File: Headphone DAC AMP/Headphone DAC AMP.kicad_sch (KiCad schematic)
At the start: 0 parts

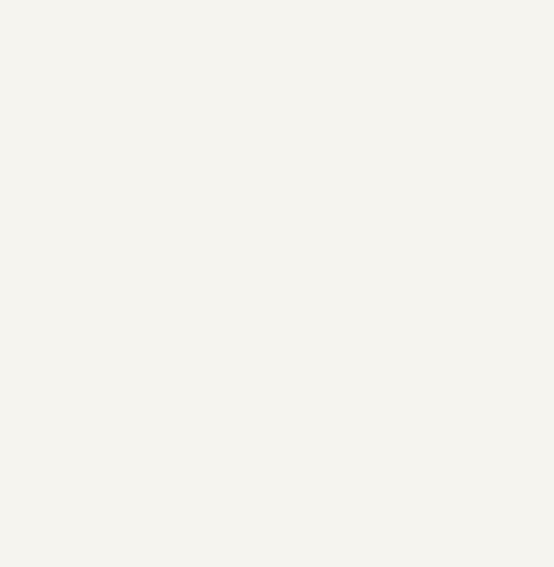
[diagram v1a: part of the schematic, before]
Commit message: Added crystals
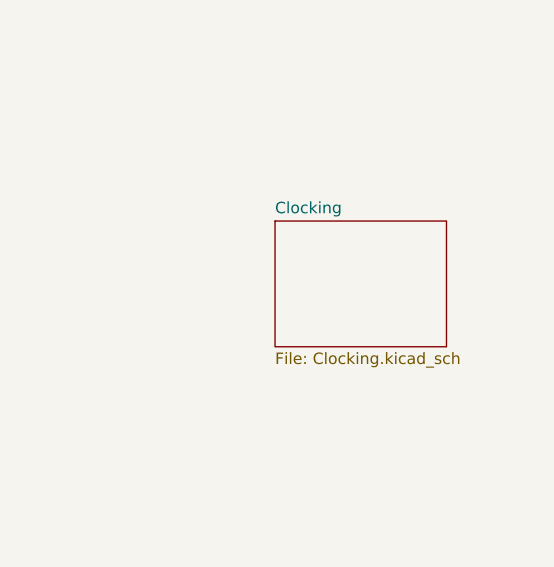
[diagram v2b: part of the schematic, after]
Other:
- added sheet Clocking (Clocking.kicad_sch)
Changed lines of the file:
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@@
+		)
+	)
+	(sheet
+		(at 203.2 72.39)
+		(size 19.05 13.97)
+		(exclude_from_sim no)
+		(in_bom yes)
+		(on_board yes)
+		(dnp no)
+		(fields_autoplaced yes)
+		(stroke
+			(width 0.1524)
+			(type solid)
+		)
+		(fill
+			(color 0 0 0 0.0000)
+		)
+		(property "Sheetname" "Clocking"
+			(at 203.2 71.6784 0)
+			(effects
+				(font
+					(size 1.27 1.27)
+				)
+				(justify left bottom)
+			)
+		)
+		(property "Sheetfile" "Clocking.kicad_sch"
+			(at 203.2 86.9446 0)
+			(effects
+				(font
+					(size 1.27 1.27)
+				)
+				(justify left top)
+			)
+		)
+		(instances
+			(project "Headphone DAC AMP"
+				(path "/d034eddd-efbc-47be-a25c-37cbfbab4cd8"
+					(page "7")
+				)
+			)
 		)
 	)

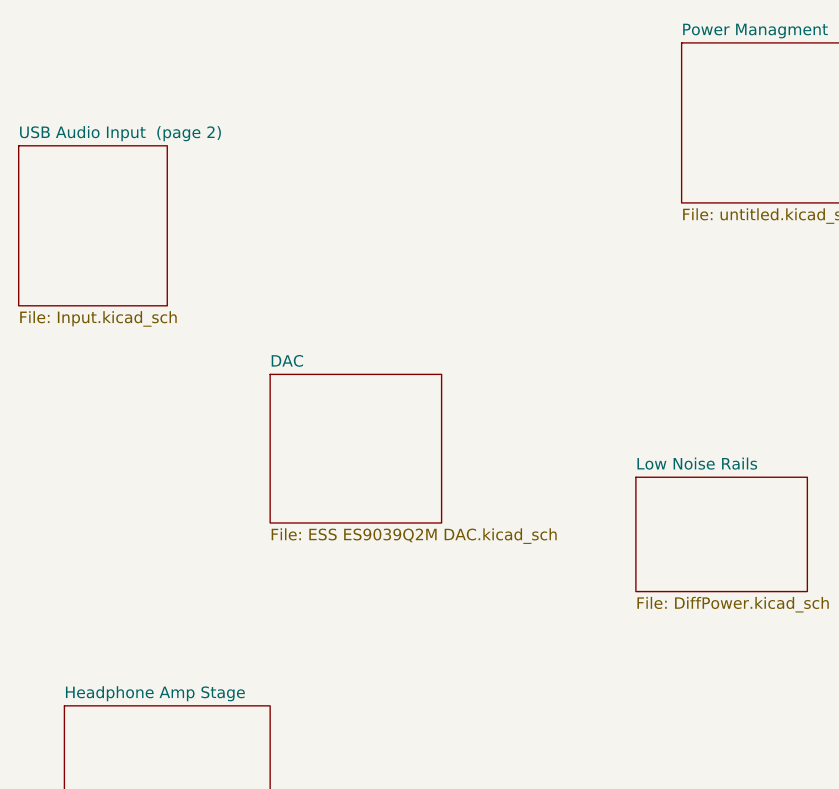
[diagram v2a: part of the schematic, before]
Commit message: Began connecting Root page
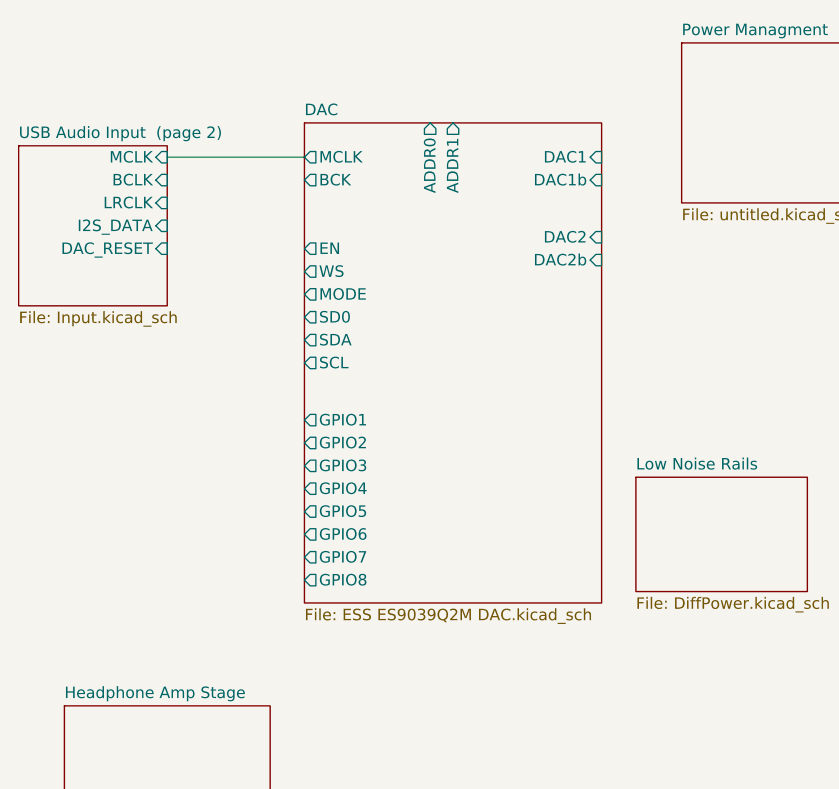
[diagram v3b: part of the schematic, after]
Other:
- sheet DAC ports: added ADDR0, ADDR1, BCK, DAC1, DAC1b, DAC2, DAC2b, EN, GPIO1, GPIO2, GPIO3, GPIO4, GPIO5, GPIO6, GPIO7, GPIO8, MCLK, MODE, SCL, SD0, SDA, WS; removed none
- sheet USB Audio Input  (page 2) ports: added BCLK, DAC_RESET, I2S_DATA, LRCLK, MCLK; removed none

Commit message: Populated pins a bit more
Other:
- sheet USB Audio Input  (page 2) renamed USB Audio Input
- sheet USB Audio Input ports: added 4D0, 4D1, 4D2, 4D3, EN45, EN_49, JTAG_TCK, JTAG_TD0, JTAG_TDI, JTAG_TMS, MISO, SCL, SDA/MOSI, SS; removed none
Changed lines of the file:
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@@
+	(wire
+		(pts
+			(xy 72.39 62.23) (xy 87.63 62.23)
+		)
+		(stroke
+			(width 0)
+			(type default)
+		)
+	)
+	(wire
+		(pts
+			(xy 72.39 69.85) (xy 87.63 69.85)
+		)
+		(stroke
+			(width 0)
+			(type default)
+		)
+	)
 	(wire
 		(pts
@@
 	(sheet
 		(at 55.88 58.42)
-		(size 16.51 17.78)
+		(size 16.51 54.61)
 		(exclude_from_sim no)
 		(in_bom yes)
@@
 			(color 0 0 0 0.0000)
 		)
-		(property "Sheetname" "USB Audio Input  (page 2)"
+		(property "Sheetname" "USB Audio Input"
 			(at 55.88 57.7084 0)
 			(effects
@@
 		)
 		(property "Sheetfile" "Input.kicad_sch"
-			(at 55.88 76.7846 0)
+			(at 55.88 113.6146 0)
 			(effects
 				(font
@@
 		(pin "DAC_RESET" input
 			(at 72.39 69.85 0)
+			(effects
+				(font
+					(size 1.27 1.27)
+				)
+				(justify right)
+			)
+		)
+		(pin "EN_49" input
+			(at 63.5 58.42 90)
+			(effects
+				(font
+					(size 1.27 1.27)
+				)
+				(justify right)
+			)
+		)
+		(pin "EN45" input
+			(at 60.96 58.42 90)
+			(effects
+				(font
+					(size 1.27 1.27)
+				)
+				(justify right)
+			)
+		)
+		(pin "JTAG_TDI" input
+			(at 72.39 99.06 0)
+			(effects
+				(font
+					(size 1.27 1.27)
+				)
+				(justify right)
+			)
+		)
+		(pin "4D2" input
+			(at 72.39 106.68 0)
+			(effects
+				(font
+					(size 1.27 1.27)
+				)
+				(justify right)
+			)
+		)
+		(pin "4D0" input
+			(at 72.39 101.6 0)
+			(effects
+				(font
+					(size 1.27 1.27)
+				)
+				(justify right)
+			)
+		)
+		(pin "JTAG_TMS" input
+			(at 72.39 93.98 0)
+			(effects
+				(font
+					(size 1.27 1.27)
+				)
+				(justify right)
+			)
+		)
+		(pin "JTAG_TD0" input
+			(at 72.39 96.52 0)
+			(effects
+				(font
+					(size 1.27 1.27)
+				)
+				(justify right)
+			)
+		)
+		(pin "JTAG_TCK" input
+			(at 72.39 91.44 0)
+			(effects
+				(font
+					(size 1.27 1.27)
+				)
+				(justify right)
+			)
+		)
+		(pin "4D1" input
+			(at 72.39 104.14 0)
+			(effects
+				(font
+					(size 1.27 1.27)
+				)
+				(justify right)
+			)
+		)
+		(pin "4D3" input
+			(at 72.39 109.22 0)
+			(effects
+				(font
+					(size 1.27 1.27)
+				)
+				(justify right)
+			)
+		)
+		(pin "MISO" input
+			(at 72.39 80.01 0)
+			(effects
+				(font
+					(size 1.27 1.27)
+				)
+				(justify right)
+			)
+		)
+		(pin "SCL" input
+			(at 72.39 72.39 0)
+			(effects
+				(font
+					(size 1.27 1.27)
+				)
+				(justify right)
+			)
+		)
+		(pin "SDA{slash}MOSI" input
+			(at 72.39 74.93 0)
+			(effects
+				(font
+					(size 1.27 1.27)
+				)
+				(justify right)
+			)
+		)
+		(pin "SS" input
+			(at 72.39 77.47 0)
 			(effects
 				(font
@@
 		)
 		(pin "SD0" output
-			(at 87.63 77.47 180)
+			(at 87.63 67.31 180)
 			(effects
 				(font
@@
 		)
 		(pin "WS" output
-			(at 87.63 72.39 180)
-			(effects
-				(font
+			(at 87.63 64.77 180)
+			(effects
+				(font

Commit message: Power updated
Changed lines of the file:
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@@
+	(wire
+		(pts
+			(xy 72.39 67.31) (xy 87.63 67.31)
+		)
+		(stroke
+			(width 0)
+			(type default)
+		)
+	)
 	(wire
 		(pts
@@
 		)
 		(stroke
+			(width 0)
+			(type default)
+		)
+	)
+	(wire
+		(pts
+			(xy 72.39 64.77) (xy 87.63 64.77)
+		)
+		(stroke

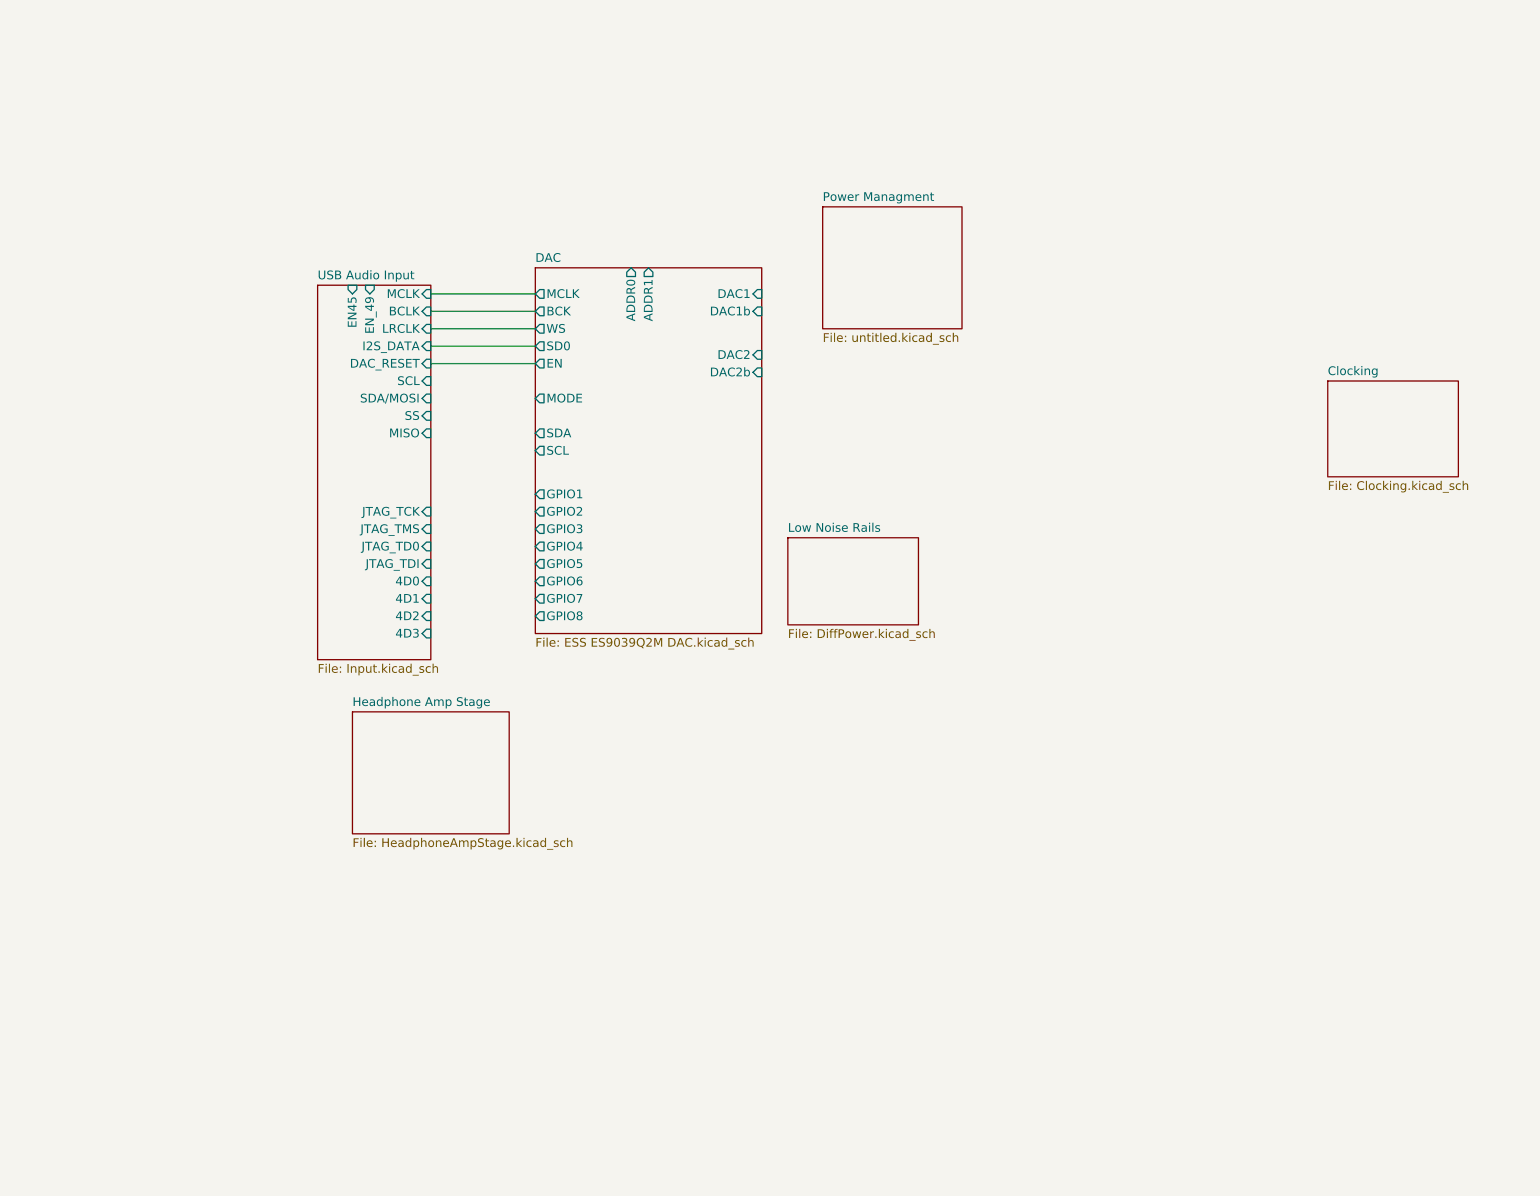
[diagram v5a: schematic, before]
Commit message: Finished AMP Stage
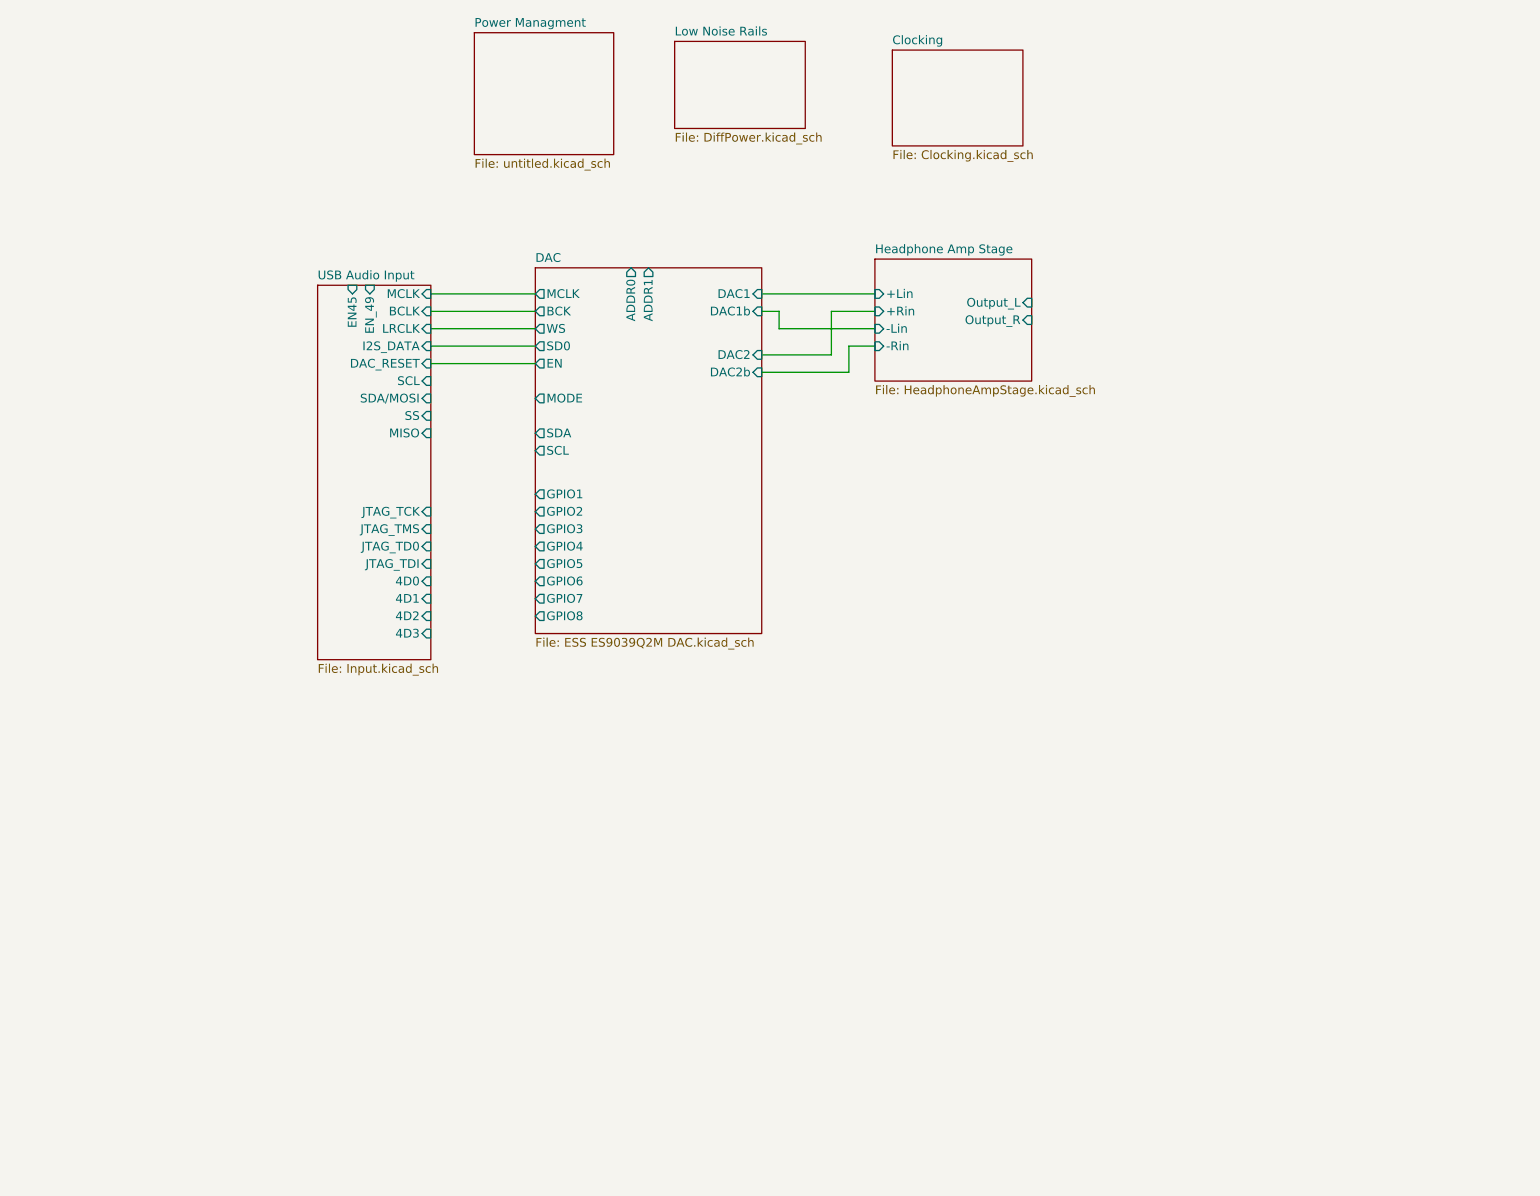
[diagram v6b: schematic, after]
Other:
- sheet Headphone Amp Stage ports: added +Lin, +Rin, -Lin, -Rin, Output_L, Output_R; removed none
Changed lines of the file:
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@@
+	(wire
+		(pts
+			(xy 133.35 67.31) (xy 137.16 67.31)
+		)
+		(stroke
+			(width 0)
+			(type default)
+		)
+	)
+	(wire
+		(pts
+			(xy 120.65 71.12) (xy 133.35 71.12)
+		)
+		(stroke
+			(width 0)
+			(type default)
+		)
+	)
+	(wire
+		(pts
+			(xy 120.65 59.69) (xy 137.16 59.69)
+		)
+		(stroke
+			(width 0)
+			(type default)
+		)
+	)
 	(wire
 		(pts
@@
 	(wire
 		(pts
+			(xy 130.81 62.23) (xy 137.16 62.23)
+		)
+		(stroke
+			(width 0)
+			(type default)
+		)
+	)
+	(wire
+		(pts
 			(xy 72.39 69.85) (xy 87.63 69.85)
 		)
@@
 	(wire
 		(pts
+			(xy 130.81 68.58) (xy 130.81 62.23)
+		)
+		(stroke
+			(width 0)
+			(type default)
+		)
+	)
+	(wire
+		(pts
+			(xy 123.19 64.77) (xy 137.16 64.77)
+		)
+		(stroke
+			(width 0)
+			(type default)
+		)
+	)
+	(wire
+		(pts
 			(xy 72.39 64.77) (xy 87.63 64.77)
 		)
@@
 	(wire
 		(pts
+			(xy 120.65 68.58) (xy 130.81 68.58)
+		)
+		(stroke
+			(width 0)
+			(type default)
+		)
+	)
+	(wire
+		(pts
+			(xy 133.35 71.12) (xy 133.35 67.31)
+		)
+		(stroke
+			(width 0)
+			(type default)
+		)
+	)
+	(wire
+		(pts
+			(xy 120.65 62.23) (xy 123.19 62.23)
+		)
+		(stroke
+			(width 0)
+			(type default)
+		)
+	)
+	(wire
+		(pts
+			(xy 123.19 62.23) (xy 123.19 64.77)
+		)
+		(stroke
+			(width 0)
+			(type default)
+		)
+	)
+	(wire
+		(pts
 			(xy 72.39 59.69) (xy 87.63 59.69)
 		)
@@
 	)
 	(sheet
-		(at 129.54 46.99)
+		(at 78.74 21.59)
 		(size 20.32 17.78)
 		(exclude_from_sim no)
@@
 		)
 		(property "Sheetname" "Power Managment"
-			(at 129.54 46.2784 0)
+			(at 78.74 20.8784 0)
 			(effects
 				(font
@@
 		)
 		(property "Sheetfile" "untitled.kicad_sch"
-			(at 129.54 65.3546 0)
+			(at 78.74 39.9546 0)
 			(effects
 				(font
@@
 	)
 	(sheet
-		(at 124.46 95.25)
+		(at 107.95 22.86)
 		(size 19.05 12.7)
 		(exclude_from_sim no)
@@
 		)
 		(property "Sheetname" "Low Noise Rails"
-			(at 124.46 94.5384 0)
+			(at 107.95 22.1484 0)
 			(effects
 				(font
@@
 		)
 		(property "Sheetfile" "DiffPower.kicad_sch"
-			(at 124.46 108.5346 0)
+			(at 107.95 36.1446 0)
 			(effects
 				(font
@@
 	)
 	(sheet
-		(at 60.96 120.65)
+		(at 137.16 54.61)
 		(size 22.86 17.78)
 		(exclude_from_sim no)
@@
 		)
 		(property "Sheetname" "Headphone Amp Stage"
-			(at 60.96 119.9384 0)
+			(at 137.16 53.8984 0)
 			(effects
 				(font
@@
 		)
 		(property "Sheetfile" "HeadphoneAmpStage.kicad_sch"
-			(at 60.96 139.0146 0)
+			(at 137.16 72.9746 0)
 			(effects
 				(font
@@
 				)
 				(justify left top)
+			)
+		)
+		(pin "+Lin" input
+			(at 137.16 59.69 180)
+			(effects
+				(font
+					(size 1.27 1.27)
+				)
+				(justify left)
+			)
+		)
+		(pin "+Rin" input
+			(at 137.16 62.23 180)
+			(effects
+				(font
+					(size 1.27 1.27)
+				)
+				(justify left)
+			)
+		)
+		(pin "-Lin" input
+			(at 137.16 64.77 180)
+			(effects
+				(font
+					(size 1.27 1.27)
+				)
+				(justify left)
+			)
+		)
+		(pin "-Rin" input
+			(at 137.16 67.31 180)
+			(effects
+				(font
+					(size 1.27 1.27)
+				)
+				(justify left)
+			)
+		)
+		(pin "Output_L" input
+			(at 160.02 60.96 0)
+			(effects
+				(font
+					(size 1.27 1.27)
+				)
+				(justify right)
+			)
+		)
+		(pin "Output_R" input
+			(at 160.02 63.5 0)
+			(effects
+				(font
+					(size 1.27 1.27)
+				)
+				(justify right)
 			)
 		)
@@
 	)
 	(sheet
-		(at 203.2 72.39)
+		(at 139.7 24.13)
 		(size 19.05 13.97)
 		(exclude_from_sim no)
@@
 		)
 		(property "Sheetname" "Clocking"
-			(at 203.2 71.6784 0)
+			(at 139.7 23.4184 0)
 			(effects
 				(font
@@
 		)
 		(property "Sheetfile" "Clocking.kicad_sch"
-			(at 203.2 86.9446 0)
-			(effects
-				(font
+			(at 139.7 38.6846 0)
+			(effects
+				(font
